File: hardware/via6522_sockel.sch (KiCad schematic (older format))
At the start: 3 parts, among them P2 VIA_PIN_1-20, P3 DIL40, P4 VIA_PIN_21-40

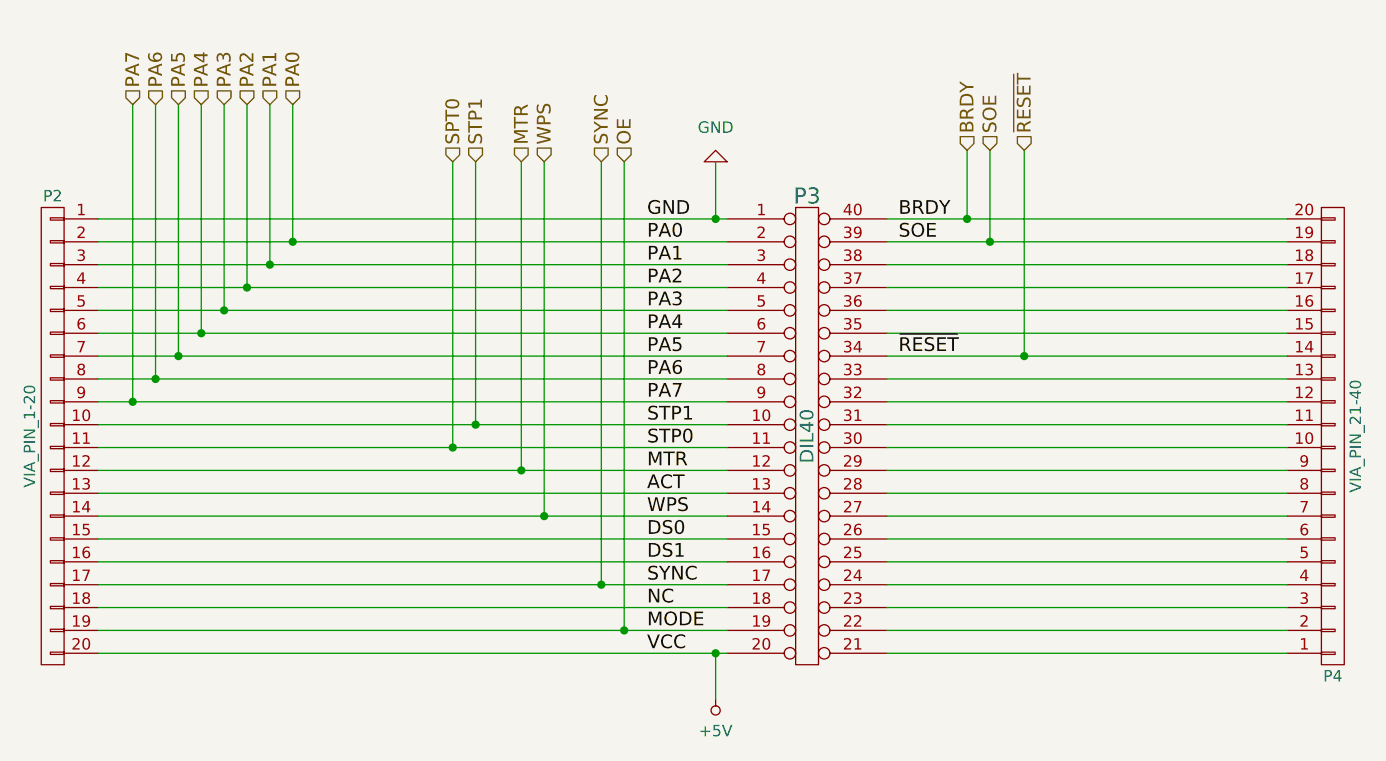
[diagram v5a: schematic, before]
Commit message: Jumper für EXT_5V hinzugefügt. Schaltplan aufgeräumt. Schaltplan auf Revision 1.3.3 gesetzt.
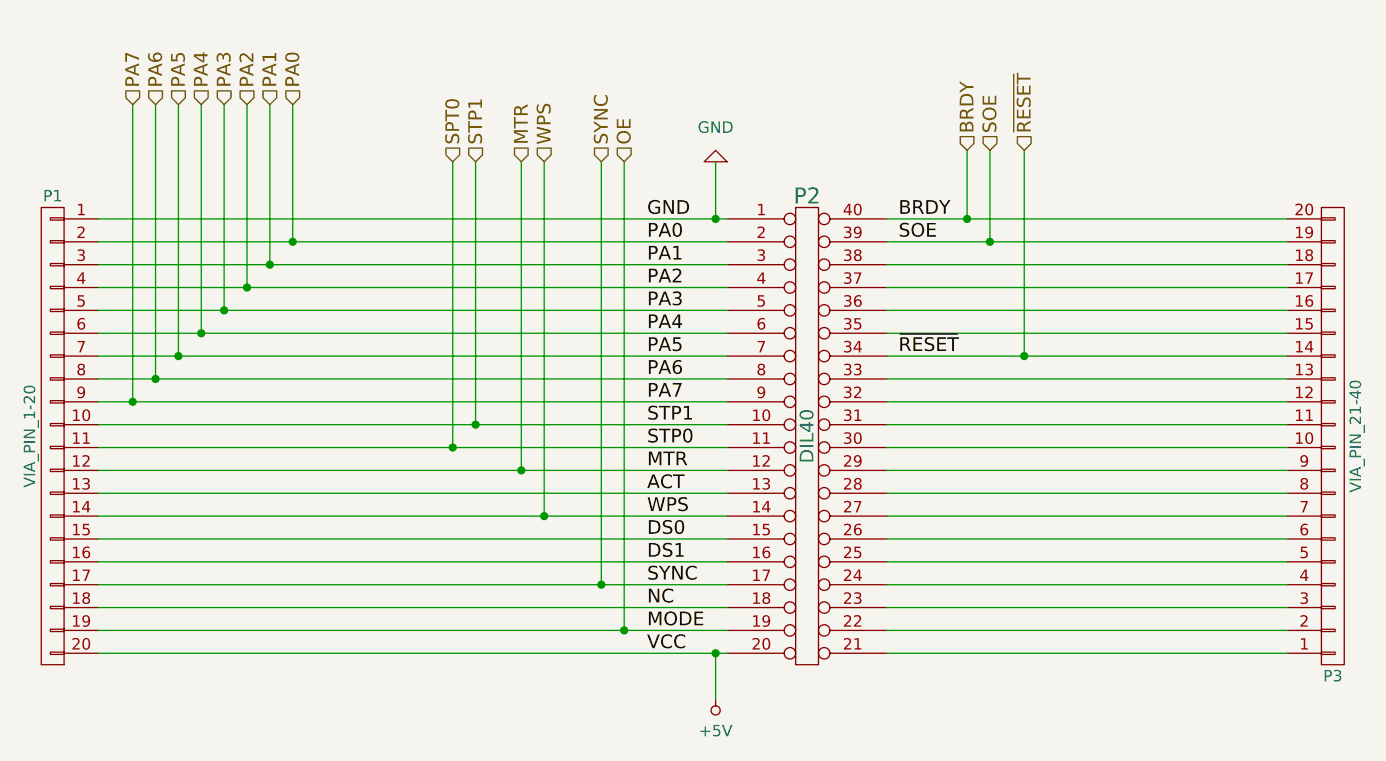
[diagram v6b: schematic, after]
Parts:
- renumbered P2 to P1, P3 to P2, P4 to P3
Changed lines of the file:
@@
 Title "1541-rebuid"
 Date "2018-05-06"
-Rev "1.3.2"
+Rev "1.3.3"
 Comp ""
 Comment1 "Erstellt: von: Thorsten Kattanek"
@@
 $EndDescr
 $Comp
-L DIL40 P3
+L DIL40 P2
 U 1 1 55F9CFCC
 P 6400 3850
-F 0 "P3" H 6400 4900 70  0000 C CNN
+F 0 "P2" H 6400 4900 70  0000 C CNN
 F 1 "DIL40" V 6400 3850 60  0000 C CNN
 F 2 "w_pth_circuits:dil_40-600_socket" H 6400 3850 60  0001 C CNN
@@
 $EndComp
 $Comp
-L CONN_01X20 P4
+L CONN_01X20 P3
 U 1 1 55F9DAC3
 P 8700 3850
-F 0 "P4" H 8700 4900 50  0000 C CNN
+F 0 "P3" H 8700 4900 50  0000 C CNN
 F 1 "VIA_PIN_21-40" V 8800 3850 50  0000 C CNN
 F 2 "Pin_Headers:Pin_Header_Straight_1x20" H 8700 3850 60  0001 C CNN
@@
 $EndComp
 $Comp
-L CONN_01X20 P2
+L CONN_01X20 P1
 U 1 1 55F9DB72
 P 3100 3850
-F 0 "P2" H 3100 4900 50  0000 C CNN
+F 0 "P1" H 3100 4900 50  0000 C CNN
 F 1 "VIA_PIN_1-20" V 3200 3850 50  0000 C CNN
 F 2 "Pin_Headers:Pin_Header_Straight_1x20" H 3100 3850 60  0001 C CNN
@@
 BRDY
 $Comp
-L GND #PWR19
+L GND #PWR21
 U 1 1 55F9667E
 P 6000 2650
-F 0 "#PWR19" H 6000 2400 50  0001 C CNN
+F 0 "#PWR21" H 6000 2400 50  0001 C CNN
 F 1 "GND" H 6000 2500 50  0000 C CNN
 F 2 "" H 6000 2650 60  0000 C CNN
@@
 $EndComp
 $Comp
-L +5V #PWR20
+L +5V #PWR22
 U 1 1 55F96755
 P 6000 5000
-F 0 "#PWR20" H 6000 4850 50  0001 C CNN
+F 0 "#PWR22" H 6000 4850 50  0001 C CNN
 F 1 "+5V" H 6000 5140 50  0000 C CNN
 F 2 "" H 6000 5000 60  0000 C CNN

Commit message: Allen Bauteilen Footprints zugeordnet.
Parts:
- P1, P3: footprint Pin_Headers:Pin_Header_Straight_1x20 -> Pin_Headers:Pin_Header_Straight_1x20_Pitch2.54mm
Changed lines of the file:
@@
 F 0 "P3" H 8700 4900 50  0000 C CNN
 F 1 "VIA_PIN_21-40" V 8800 3850 50  0000 C CNN
-F 2 "Pin_Headers:Pin_Header_Straight_1x20" H 8700 3850 60  0001 C CNN
+F 2 "Pin_Headers:Pin_Header_Straight_1x20_Pitch2.54mm" H 8700 3850 60  0001 C CNN
 F 3 "" H 8700 3850 60  0000 C CNN
 	1    8700 3850
@@
 F 0 "P1" H 3100 4900 50  0000 C CNN
 F 1 "VIA_PIN_1-20" V 3200 3850 50  0000 C CNN
-F 2 "Pin_Headers:Pin_Header_Straight_1x20" H 3100 3850 60  0001 C CNN
+F 2 "Pin_Headers:Pin_Header_Straight_1x20_Pitch2.54mm" H 3100 3850 60  0001 C CNN
 F 3 "" H 3100 3850 60  0000 C CNN
 	1    3100 3850
